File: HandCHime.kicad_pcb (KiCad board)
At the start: 4 copper layers, 38.1 x 22.6 mm, 18 parts, among them J1 USB_C_Receptacle_USB2.0, J2 Pins, SW0 BOOT, SW1 Row 0, Col 0, SW2 Row 0, Col 1, U1 CH552T, U2 PRTR5V0U2X

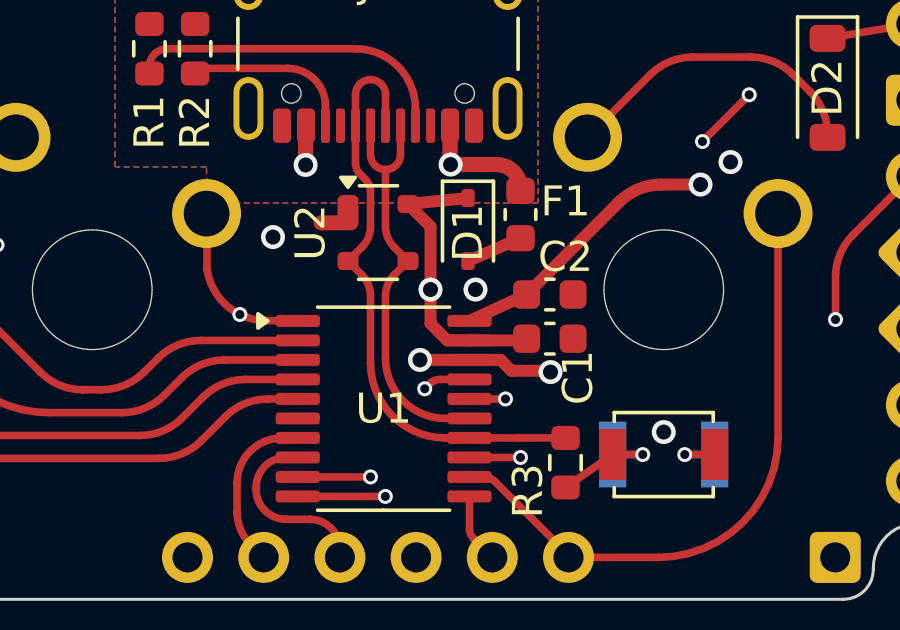
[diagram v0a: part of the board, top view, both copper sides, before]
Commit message: Swap Row from P1.3 to P1.2 for better routing
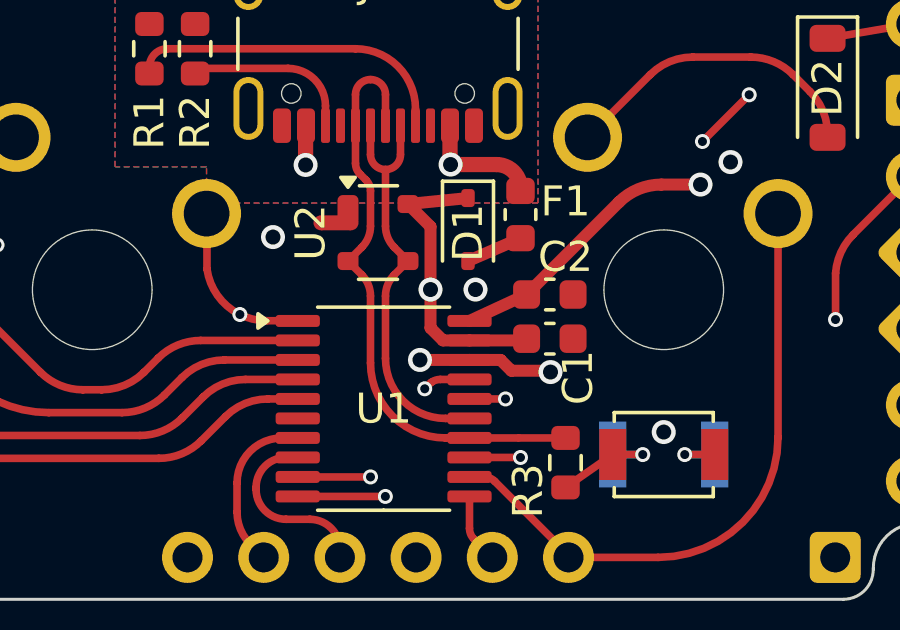
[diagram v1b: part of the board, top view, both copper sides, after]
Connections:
- J2 pad 12: P12 -> P13
- U1 pad 16: R0 -> P13
- U1 pad 17: P12 -> R0
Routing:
- net P13: track 0.00 -> 12.0 mm, vias 0 -> 1
- net P12: track 11.2 -> 0.00 mm, vias 1 -> 0
- net R0: track 59.0 -> 57.9 mm
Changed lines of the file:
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@@
 	(net 11 "Net-(D3-A)")
 	(net 12 "GNDPWR")
-	(net 13 "P12")
+	(net 13 "P13")
 	(net 14 "P14")
 	(net 15 "RX")
@@
 			(layers "F.Cu" "F.Paste" "F.Mask")
 			(roundrect_rratio 0.25)
-			(net 9 "R0")
+			(net 13 "P13")
 			(pinfunction "P1.3")
 			(pintype "input")
@@
 			(layers "F.Cu" "F.Paste" "F.Mask")
 			(roundrect_rratio 0.25)
-			(net 13 "P12")
+			(net 9 "R0")
 			(pinfunction "P1.2")
 			(pintype "input")
@@
 			)
 		)
-		(property "PIN12" "12"
+		(property "PIN12" "13"
 			(at 0 0 0)
 			(unlocked yes)
@@
 			(layers "*.Cu" "*.Mask")
 			(remove_unused_layers no)
-			(net 13 "P12")
+			(net 13 "P13")
 			(pinfunction "${PIN12}")
 			(pintype "input")
@@
 		(fp_arc
 			(start 6.497236 -6.998884)
-			(mid 6.850796 -6.85243)
+			(mid 6.85076 -6.852424)
 			(end 6.997236 -6.498884)
 			(stroke
@@
 		(fp_arc
 			(start 6.497236 -6.998884)
-			(mid 6.850796 -6.85243)
+			(mid 6.85076 -6.852424)
 			(end 6.997236 -6.498884)
 			(stroke
@@
 	)
 	(segment
-		(start 160.5 50)
-		(end 160.5 51.135042)
+		(start 160.916 51.696)
+		(end 161.8 51.696)
 		(width 0.4)
 		(layer "F.Cu")
@@
 	)
 	(segment
-		(start 160.5 51.135042)
-		(end 161.060958 51.696)
+		(start 160.5 50)
+		(end 160.5 51.28)
 		(width 0.4)
 		(layer "F.Cu")
@@
 	)
 	(segment
-		(start 161.060958 51.696)
-		(end 161.8 51.696)
+		(start 160.5 51.28)
+		(end 160.916 51.696)
 		(width 0.4)
 		(layer "F.Cu")
@@
 	)
 	(segment
+		(start 160.307 53.307)
+		(end 160.308918 53.307)
+		(width 0.254)
+		(layer "F.Cu")
+		(net 9)
+	)
+	(segment
 		(start 143.764 41.6263)
 		(end 140.97 41.148)
@@
 	)
 	(segment
+		(start 160.308918 53.307)
+		(end 160.518933 53.096985)
+		(width 0.254)
+		(layer "F.Cu")
+		(net 9)
+	)
+	(segment
 		(start 146.05 48.514)
 		(end 144.272 46.736)
@@
 	)
 	(segment
-		(start 163 53.646)
-		(end 161.8 53.646)
+		(start 160.825107 52.996)
+		(end 161.8 52.996)
 		(width 0.254)
 		(layer "F.Cu")
@@
 	)
 	(via
-		(at 146.05 48.514)
+		(at 160.307 53.307)
 		(size 0.5)
 		(drill 0.3)
@@
 	)
 	(via
-		(at 144.272 46.736)
+		(at 146.05 48.514)
 		(size 0.5)
 		(drill 0.3)
@@
 	)
 	(via
-		(at 163 53.646)
+		(at 144.272 46.736)
 		(size 0.5)
 		(drill 0.3)
@@
 		(net 9)
 	)
-	(segment
-		(start 163.5 53.146)
-		(end 163 53.646)
+	(arc
+		(start 160.518933 53.096985)
+		(mid 160.664387 53.022533)
+		(end 160.825107 52.996)
 		(width 0.254)
-		(layer "In2.Cu")
+		(layer "F.Cu")
 		(net 9)
 	)
 	(segment
-		(start 162.646 53.646)
-		(end 160.25 51.25)
+		(start 153.27943 50.17457)
+		(end 155.58457 50.17457)
 		(width 0.254)
 		(layer "In2.Cu")
@@
 	)
 	(segment
-		(start 160.25 51.25)
-		(end 155.898 51.25)
+		(start 146.05 51.054)
+		(end 147.828 52.832)
 		(width 0.254)
 		(layer "In2.Cu")
@@
 	)
 	(segment
-		(start 154.82257 50.17457)
-		(end 153.27943 50.17457)
+		(start 144.272 44.45)
+		(end 140.97 41.148)
 		(width 0.254)
 		(layer "In2.Cu")
@@
 	)
 	(segment
-		(start 163.5 51.13)
-		(end 163.5 53.146)
+		(start 155.58457 50.17457)
+		(end 158.717 53.307)
 		(width 0.254)
 		(layer "In2.Cu")
@@
 	)
 	(segment
-		(start 144.272 44.45)
-		(end 140.97 41.148)
+		(start 147.828 52.832)
+		(end 150.622 52.832)
 		(width 0.254)
 		(layer "In2.Cu")
@@
 	)
 	(segment
-		(start 163 53.646)
-		(end 162.646 53.646)
+		(start 173.482 41.148)
+		(end 176.53 41.148)
 		(width 0.254)
 		(layer "In2.Cu")
@@
 	)
 	(segment
-		(start 150.622 52.832)
-		(end 147.828 52.832)
+		(start 144.272 46.736)
+		(end 144.272 44.45)
 		(width 0.254)
 		(layer "In2.Cu")
@@
 	)
 	(segment
-		(start 147.828 52.832)
+		(start 146.05 48.514)
 		(end 146.05 51.054)
 		(width 0.254)
@@
 	)
 	(segment
-		(start 173.482 41.148)
-		(end 176.53 41.148)
-		(width 0.254)
-		(layer "In2.Cu")
-		(net 9)
-	)
-	(segment
-		(start 144.272 46.736)
-		(end 144.272 44.45)
+		(start 158.717 53.307)
+		(end 160.307 53.307)
 		(width 0.254)
 		(layer "In2.Cu")
@@
 	)
 	(segment
-		(start 155.898 51.25)
-		(end 154.82257 50.17457)
+		(start 169.565 45.065)
+		(end 163.5 51.13)
 		(width 0.254)
 		(layer "In2.Cu")
@@
 	)
 	(segment
-		(start 169.565 45.065)
+		(start 161.323 53.307)
 		(end 163.5 51.13)
 		(width 0.254)
@@
 	)
 	(segment
-		(start 153.27943 50.17457)
-		(end 150.622 52.832)
+		(start 171.122556 43.507444)
+		(end 173.482 41.148)
 		(width 0.254)
 		(layer "In2.Cu")
@@
 	)
 	(segment
-		(start 146.05 51.054)
-		(end 146.05 48.514)
+		(start 160.307 53.307)
+		(end 161.323 53.307)
 		(width 0.254)
 		(layer "In2.Cu")
@@
 	)
 	(segment
-		(start 171.122556 43.507444)
-		(end 173.482 41.148)
+		(start 150.622 52.832)
+		(end 153.27943 50.17457)
 		(width 0.254)
 		(layer "In2.Cu")
@@
 	)
 	(segment
-		(start 160.307 53.307)
-		(end 160.308918 53.307)
-		(width 0.254)
-		(layer "F.Cu")
-		(net 13)
-	)
-	(segment
-		(start 160.308918 53.307)
-		(end 160.518933 53.096985)
-		(width 0.254)
-		(layer "F.Cu")
-		(net 13)
-	)
-	(segment
-		(start 160.825107 52.996)
-		(end 161.8 52.996)
+		(start 163 53.646)
+		(end 161.8 53.646)
 		(width 0.254)
 		(layer "F.Cu")
@@
 	)
 	(via
-		(at 160.307 53.307)
+		(at 163 53.646)
 		(size 0.5)
 		(drill 0.3)
@@
 		(net 13)
 	)
-	(arc
-		(start 160.518933 53.096985)
-		(mid 160.664387 53.022533)
-		(end 160.825107 52.996)
+	(segment
+		(start 162.036 54.61)
+		(end 158.75 54.61)
 		(width 0.254)
-		(layer "F.Cu")
+		(layer "In2.Cu")
 		(net 13)
 	)
 	(segment
-		(start 160.307 53.307)
-		(end 158.443 53.307)
+		(start 158.75 54.61)
+		(end 157.48 55.88)
 		(width 0.254)
 		(layer "In2.Cu")
@@
 	)
 	(segment
-		(start 159.512 58.928)
-		(end 160.02 58.928)
+		(start 157.48 56.896)
+		(end 159.512 58.928)
 		(width 0.254)
 		(layer "In2.Cu")
@@
 	)
 	(segment
-		(start 157 56.416)
-		(end 159.512 58.928)
+		(start 159.512 58.928)
+		(end 160.02 58.928)
 		(width 0.254)
 		(layer "In2.Cu")
@@
 	)
 	(segment
-		(start 158.443 53.307)
-		(end 157 54.75)
+		(start 163 53.646)
+		(end 162.036 54.61)
 		(width 0.254)
 		(layer "In2.Cu")
@@
 	)
 	(segment
-		(start 157 54.75)
-		(end 157 56.416)
+		(start 157.48 55.88)
+		(end 157.48 56.896)
 		(width 0.254)
 		(layer "In2.Cu")

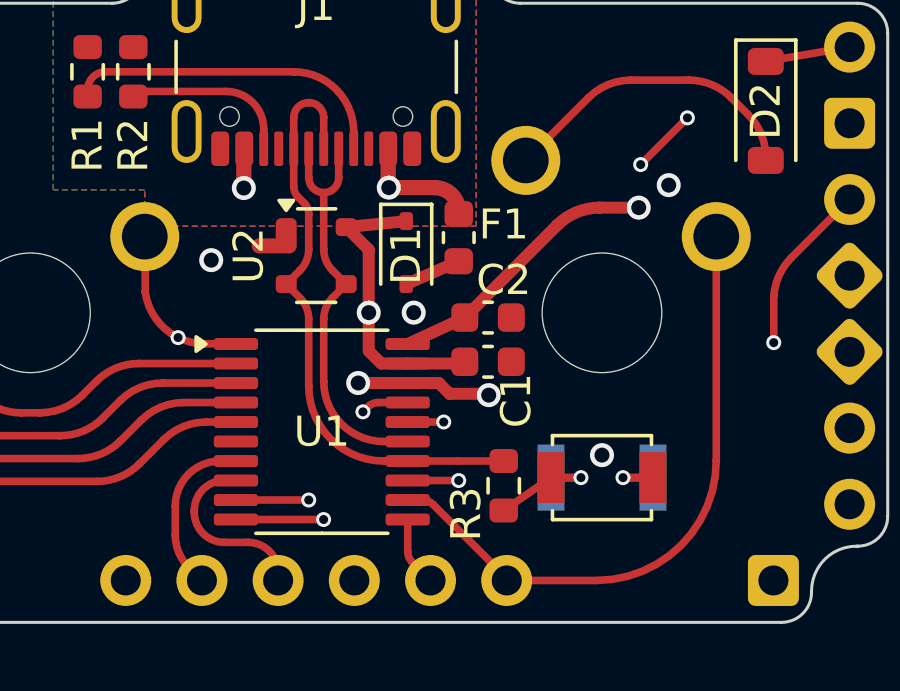
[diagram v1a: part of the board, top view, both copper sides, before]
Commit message: Minor tweaks
 * Round pads on boot button
 * Add back silkscreen for boot button
 * Improve pad size for Schottky diode (D1)
 * Tune VCC routing
 * Fix DRC errors on net ties
 * Fix board constraints to remove DRC errors on vias
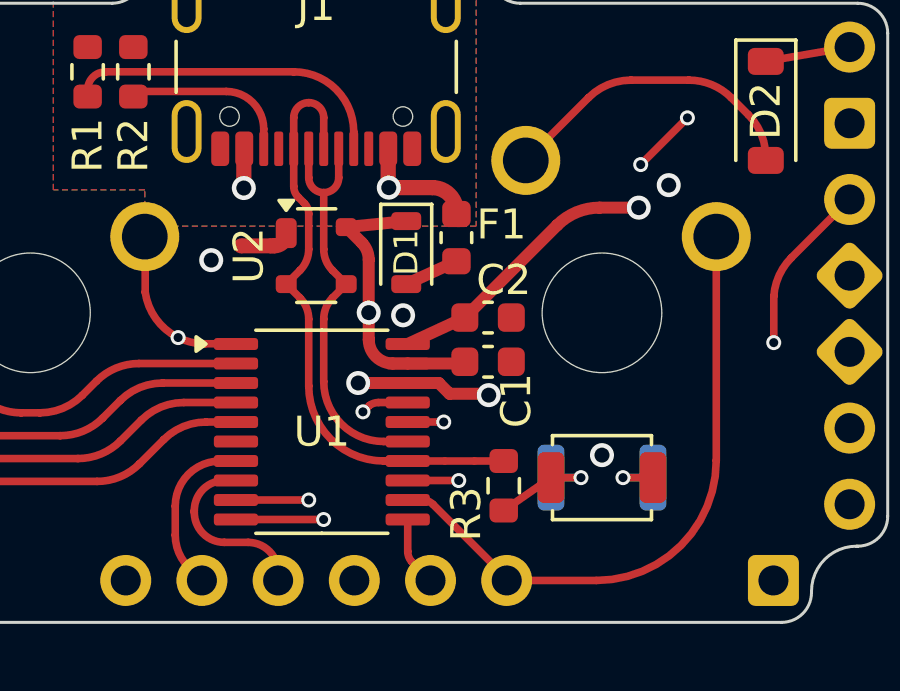
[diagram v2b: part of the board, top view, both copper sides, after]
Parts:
- D1: footprint Diode_SMD:D_SOD-323 -> Project Library:D_SOD-323
- moved NT1 0.61 mm to (156.7, 47.8)
- moved NT2 0.59 mm to (163.5, 54.9)
- moved F1 0.08 mm to (163.4, 47.5)
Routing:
- net USB+: track 16.9 -> 18.1 mm
- net GNDPWR: track 0.00 -> 0.74 mm
- net BOOT: track 1.56 -> 0.97 mm
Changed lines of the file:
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@@
 	(footprint "Project Library:NetTie-2_SMD_Pad0.254mm"
 		(layer "F.Cu")
-		(at 162.941 54.946 180)
+		(at 163.53125 54.946 180)
 		(descr "Net tie, 2 pin, 0.5mm square SMD pads")
 		(tags "net tie")
@@
 	(footprint "Fuse:Fuse_0603_1608Metric"
 		(layer "F.Cu")
-		(at 163.5 47.5 -90)
+		(at 163.4236 47.5 -90)
 		(descr "Fuse SMD 0603 (1608 Metric), square (rectangular) end terminal, IPC_7351 nominal, (Body size source: http://www.tortai-tech.com/upload/download/2011102023233369053.pdf), generated with kicad-footprint-generator")
 		(tags "fuse")
@@
 		)
 	)
-	(footprint "Diode_SMD:D_SOD-323"
+	(footprint "Project Library:D_SOD-323"
 		(layer "F.Cu")
 		(at 161.75 48 -90)
@@
 		(tags "SOD-323")
 		(property "Reference" "D1"
-			(at 0.110099 0 90)
+			(at 0 0 -90)
 			(layer "F.SilkS")
 			(effects
 				(font
-					(size 1 1)
+					(size 0.8 0.8)
 					(thickness 0.15)
 				)
@@
 		)
 		(property "Value" "PMEG2010EA"
-			(at 0.1 1.9 90)
+			(at 0.1 1.9 -90)
 			(layer "F.Fab")
 			(effects
@@
 			)
 		)
-		(property "Footprint" "Diode_SMD:D_SOD-323"
+		(property "Footprint" "Project Library:D_SOD-323"
 			(at 0 0 -90)
 			(unlocked yes)
@@
 			)
 		)
-		(property "DigiKey" "1727-4326"
-			(at 0 0 90)
+		(property "LCSC" "C2837790"
+			(at 0 0 -90)
+			(unlocked yes)
 			(layer "F.Fab")
 			(hide yes)
@@
 			)
 		)
-		(property "LCSC" "C2837790"
-			(at 0 0 90)
+		(property "DigiKey" "1727-4326"
+			(at 0 0 -90)
+			(unlocked yes)
 			(layer "F.Fab")
 			(hide yes)
@@
 		(fp_line
 			(start -0.3 0)
-			(end -0.499999 0)
+			(end -0.5 0)
 			(stroke
 				(width 0.1)
@@
 		)
 		(fp_line
-			(start 0.199999 0)
+			(start 0.2 0)
 			(end 0.45 0)
 			(stroke
@@
 		)
 		(fp_line
-			(start -0.3 -0.349999)
-			(end -0.3 0.349999)
+			(start -0.3 -0.35)
+			(end -0.3 0.35)
 			(stroke
 				(width 0.1)
@@
 		)
 		(fp_text user "${REFERENCE}"
-			(at 0 -1.850001 90)
+			(at 0 -1.85 -90)
 			(layer "F.Fab")
 			(effects
@@
 		(pad "1" smd roundrect
 			(at -1.05 0 270)
-			(size 0.6 0.45)
+			(size 0.6 1)
 			(layers "F.Cu" "F.Paste" "F.Mask")
 			(roundrect_rratio 0.25)
@@
 		(pad "2" smd roundrect
 			(at 1.05 0 270)
-			(size 0.6 0.45)
+			(size 0.6 1)
 			(layers "F.Cu" "F.Paste" "F.Mask")
 			(roundrect_rratio 0.25)
@@
 	(footprint "NetTie:NetTie-2_SMD_Pad0.5mm"
 		(layer "F.Cu")
-		(at 157.350001 47.775 180)
+		(at 156.7434 47.775 180)
 		(descr "Net tie, 2 pin, 0.5mm square SMD pads")
 		(tags "net tie")
@@
 		)
 		(fp_text user "${VALUE}"
+			(at 0 1.5 0)
+			(unlocked yes)
+			(layer "B.SilkS")
+			(effects
+				(font
+					(size 0.7 0.7)
+					(thickness 0.15)
+					(bold yes)
+				)
+				(justify top mirror)
+			)
+		)
+		(fp_text user "${VALUE}"
 			(at 0 -1.75 0)
 			(unlocked yes)
@@
 			)
 		)
-		(pad "1" smd rect
+		(pad "1" smd roundrect
 			(at -1.7 0)
 			(size 0.9 1.7)
 			(layers "F.Cu" "F.Paste" "F.Mask")
+			(roundrect_rratio 0.25)
 			(net 5 "Net-(R3-Pad2)")
 			(pinfunction "1")
 			(pintype "passive")
 		)
-		(pad "1" smd rect
+		(pad "1" smd roundrect
 			(at -1.7 0)
 			(size 0.9 2.2)
 			(layers "B.Cu" "B.Mask")
+			(roundrect_rratio 0.25)
 			(net 5 "Net-(R3-Pad2)")
 			(pinfunction "1")
 			(pintype "passive")
 		)
-		(pad "2" smd rect
+		(pad "2" smd roundrect
 			(at 1.7 0)
 			(size 0.9 1.7)
 			(layers "F.Cu" "F.Paste" "F.Mask")
+			(roundrect_rratio 0.25)
 			(net 7 "+3V3")
 			(pinfunction "2")
 			(pintype "passive")
 		)
-		(pad "2" smd rect
+		(pad "2" smd roundrect
 			(at 1.7 0)
 			(size 0.9 2.2)
 			(layers "B.Cu" "B.Mask")
+			(roundrect_rratio 0.25)
 			(net 7 "+3V3")
 			(pinfunction "2")
@@
 		(fp_arc
 			(start 6.497236 -6.998884)
-			(mid 6.85076 -6.852424)
+			(mid 6.850796 -6.85243)
 			(end 6.997236 -6.498884)
 			(stroke
@@
 		(fp_arc
 			(start 6.497236 -6.998884)
-			(mid 6.85076 -6.852424)
+			(mid 6.850796 -6.85243)
 			(end 6.997236 -6.498884)
 			(stroke
@@
 	)
 	(segment
-		(start 160.5 47.9)
+		(start 160.265685 47.665685)
 		(end 159.75 47.15)
 		(width 0.4)
@@
 	(segment
 		(start 160.5 50)
-		(end 160.5 47.9)
+		(end 160.5 48.231371)
 		(width 0.4)
 		(layer "F.Cu")
@@
 	)
 	(segment
-		(start 160.916 51.696)
+		(start 161.3 51.696)
 		(end 161.8 51.696)
 		(width 0.4)
@@
 	(segment
 		(start 160.5 50)
-		(end 160.5 51.28)
-		(width 0.4)
-		(layer "F.Cu")
-		(net 1)
-	)
-	(segment
-		(start 160.5 51.28)
-		(end 160.916 51.696)
+		(end 160.5 50.896)
 		(width 0.4)
 		(layer "F.Cu")
@@
 		(net 1)
 	)
+	(arc
+		(start 160.5 50.896)
+		(mid 160.734315 51.461685)
+		(end 161.3 51.696)
+		(width 0.4)
+		(layer "F.Cu")
+		(net 1)
+	)
+	(arc
+		(start 160.5 48.231371)
+		(mid 160.439103 47.925224)
+		(end 160.265685 47.665685)
+		(width 0.4)
+		(layer "F.Cu")
+		(net 1)
+	)
 	(segment
 		(start 152.275503 49.25)
@@
 	)
 	(via
-		(at 162 50)
+		(at 161.6456 50.0888)
 		(size 0.8)
 		(drill 0.5)
@@
 	(segment
 		(start 161.75 49.05)
-		(end 163.5 48.287501)
+		(end 163.4236 48.287501)
 		(width 0.4)
 		(layer "F.Cu")
@@
 	)
 	(segment
-		(start 163.5 46.633058)
-		(end 163.5 46.712499)
+		(start 163.4236 46.633058)
+		(end 163.4236 46.712499)
 		(width 0.508)
 		(layer "F.Cu")
@@
 	)
 	(segment
-		(start 156.337 45.847)
-		(end 156.337 44.805)
+		(start 161.168965 45.833058)
+		(end 162.6236 45.833058)
 		(width 0.508)
 		(layer "F.Cu")
@@
 	)
 	(segment
-		(start 161.168965 45.833058)
-		(end 162.7 45.833058)
+		(start 156.337 45.847)
+		(end 156.337 44.805)
 		(width 0.508)
 		(layer "F.Cu")
@@
 	)
 	(arc
-		(start 163.5 46.633058)
-		(mid 163.265685 46.067373)
-		(end 162.7 45.833058)
+		(start 163.4236 46.633058)
+		(mid 163.189285 46.067373)
+		(end 162.6236 45.833058)
 		(width 0.508)
 		(layer "F.Cu")
@@
 	)
 	(segment
+		(start 157.243399 47.775)
+		(end 157.35 47.775)
+		(width 0.5)
+		(layer "F.Cu")
+		(net 12)
+	)
+	(segment
+		(start 157.75 47.375)
+		(end 157.75 47.35)
+		(width 0.5)
+		(layer "F.Cu")
+		(net 12)
+	)
+	(arc
+		(start 157.75 47.375)
+		(mid 157.632843 47.657843)
+		(end 157.35 47.775)
+		(width 0.5)
+		(layer "F.Cu")
+		(net 12)
+	)
+	(segment
 		(start 163 53.646)
 		(end 161.8 53.646)
@@
 	)
 	(segment
-		(start 163.441 54.946)
+		(start 164.03125 54.946)
 		(end 165 54.946)
 		(width 0.254)
@@
 		(width 0.254)
 		(layer "F.Cu")
+		(net 29)
+	)
+	(segment
+		(start 161.8 54.946)
+		(end 163.03125 54.946)
+		(width 0.254)
+		(layer "F.Cu")
